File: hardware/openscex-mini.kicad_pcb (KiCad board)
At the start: 2 copper layers, 35.6 x 25.1 mm, 11 parts, among them J1 ISP, U1 ATtiny85-20PU

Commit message: feat(hardware): add a RESET pull-up to every board
The mini and bare boards now hold pin 1 high with a 10 kOhm pull-up,
as the carrier already did. The chip's own pull-up is 30 to 60 kOhm,
weak against noise coupled in from the console, and a spurious reset
costs the region check of the disc being read. Any ISP programmer
still overrides it.
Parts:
- added R2: 10k, Resistor_THT:R_Axial_DIN0204_L3.6mm_D1.6mm_P5.08mm_Horizontal, F.Cu at (125.0, 106.2)
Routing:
- net /SUBQ: track 50.8 -> 23.1 mm, vias 0 -> 2
- net /DATA: track 25.9 -> 51.3 mm, vias 1 -> 0
- net /RST: track 19.6 -> 25.2 mm
- net /VCC: track 38.0 -> 41.7 mm
- net /GND: vias 15 -> 12

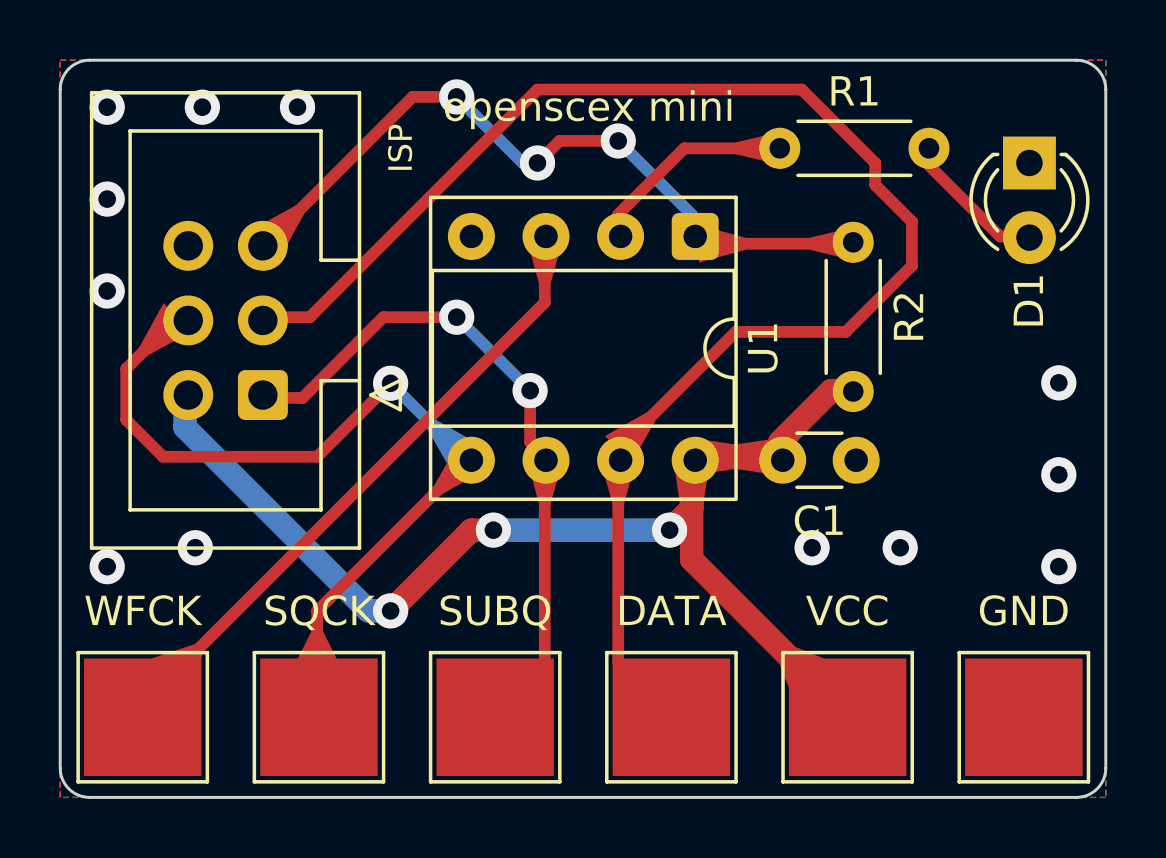
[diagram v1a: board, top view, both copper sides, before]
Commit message: feat(hardware): name datasheet-checked parts
Every BOM line now names an exact manufacturer part, each checked
against its own datasheet: Microchip ATTINY85-20PU in a TE
1-2199298-2 socket, KEMET C315C104K5R5TA, Panasonic EEU-FC1A101S,
Vishay MBA0204 resistors, onsemi 2N3904RLRAG and 1N4148TR,
Kingbright WP710A10ID, CTS 206-2ST, Same Sky CMI-1295IC-0385T and
Wurth 61200621621.

C1 moves to a 4.0 x 2.5 mm footprint that fits the KEMET body. A
project footprint library, hardware/openscex.pretty, carries the hole
sizes the Wurth header and the buzzer datasheets recommend, 1.1 mm and
0.8 mm in 2 mm pads.
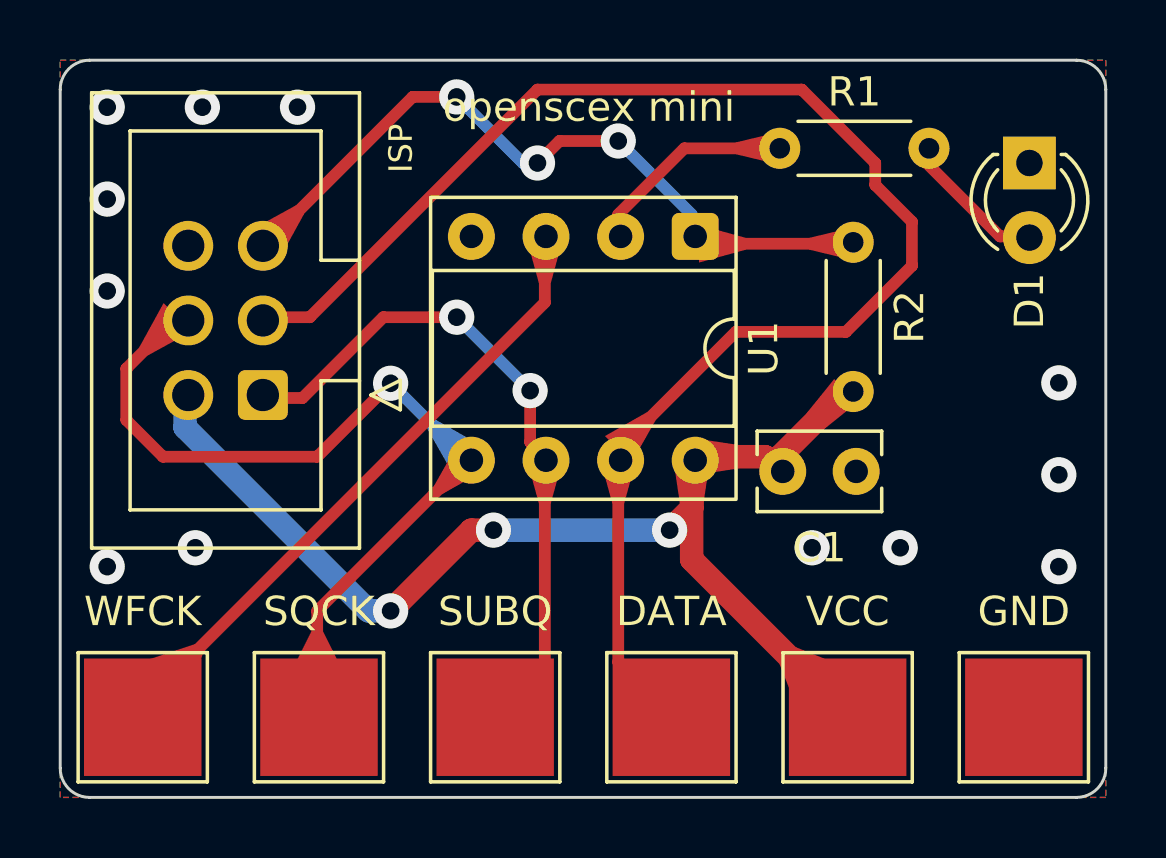
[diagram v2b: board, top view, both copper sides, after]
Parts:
- C1: footprint Capacitor_THT:C_Disc_D3.0mm_W1.6mm_P2.50mm -> Capacitor_THT:C_Rect_L4.0mm_W2.5mm_P2.50mm
- J1: footprint Connector_IDC:IDC-Header_2x03_P2.54mm_Vertical -> openscex:IDC-Header_2x03_P2.54mm_Vertical_Wurth_61200621621
- moved C1 0.38 mm to (122.6, 114.0)
